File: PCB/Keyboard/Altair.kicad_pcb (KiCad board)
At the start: 2 copper layers, 57 parts, among them SW1 SW_Push, SW10 SW_Push, SW11 SW_Push, SW12 SW_Push, SW13 SW_Push, SW14 SW_Push, SW15 SW_Push, SW16 SW_Push, SW17 SW_Push, SW18 SW_Push, SW19 SW_Push, SW2 SW_Push, SW20 SW_Push, SW21 SW_Push, SW22 SW_Push, SW23 SW_Push, SW24 SW_Push, SW25 SW_Push, SW26 SW_Push, SW27 SW_Push, SW28 SW_Push, SW3 SW_Push, SW4 SW_Push, SW5 SW_Push, SW6 SW_Push, SW7 SW_Push, SW8 SW_Push, SW9 SW_Push, U1 SuperMini nRF52840

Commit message: add hs reverse fp
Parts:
- moved D4 6.87 mm to (144.4, 53.9)
- moved D3 6.52 mm to (125.1, 56.1)
- moved D12 6.02 mm to (181.7, 77.2)
- moved D11 5.94 mm to (162.4, 74.9)
- moved D5 5.21 mm to (162.9, 54.7)
- moved D6 4.64 mm to (181.6, 56.5)
- moved D1 2.24 mm to (84.6, 60.6)
- moved D2 1.94 mm to (87.2, 60.7)
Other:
- board outline added: 137.3 x 110.5 mm

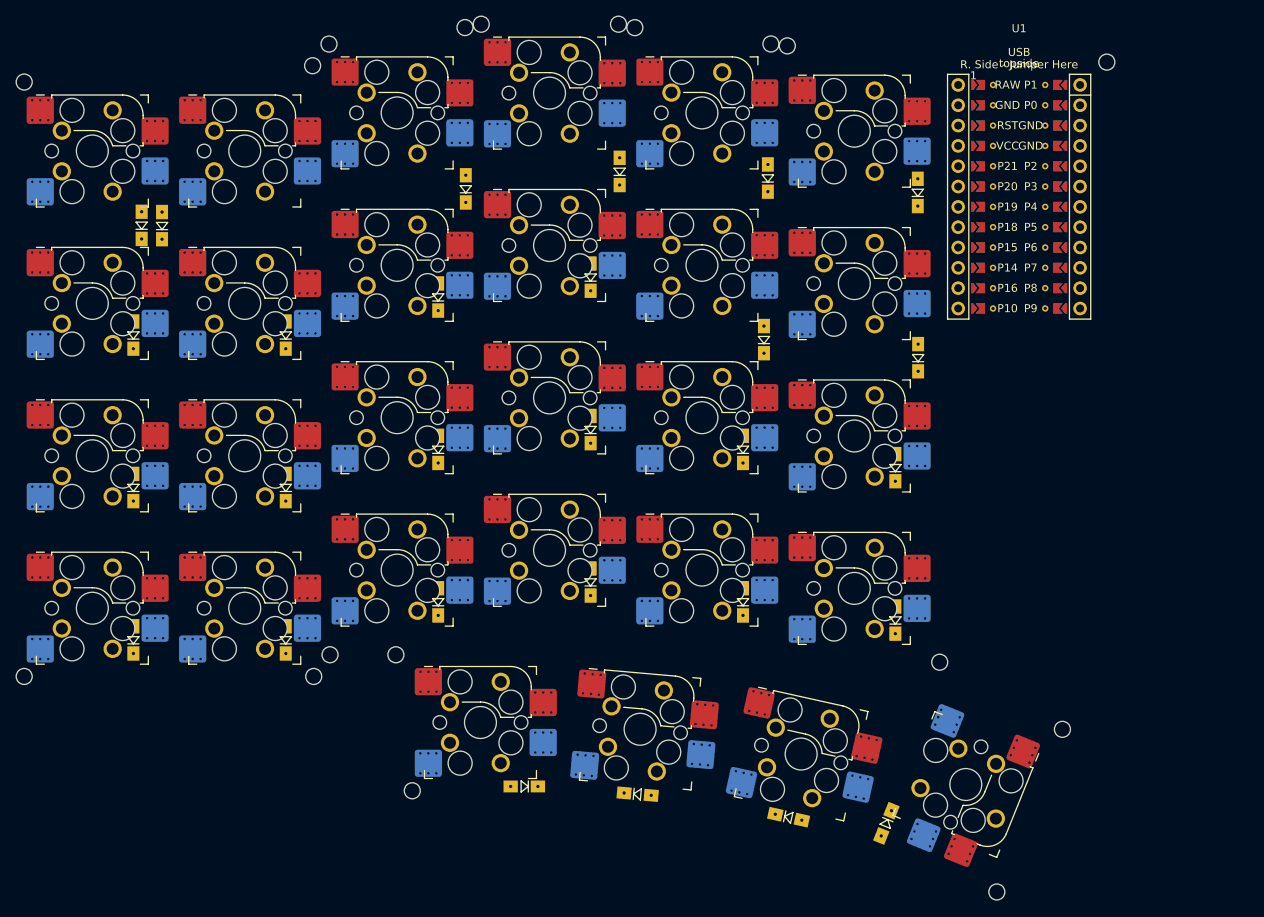
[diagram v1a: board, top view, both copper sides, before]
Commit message: Done outline and fp for mcu/switch
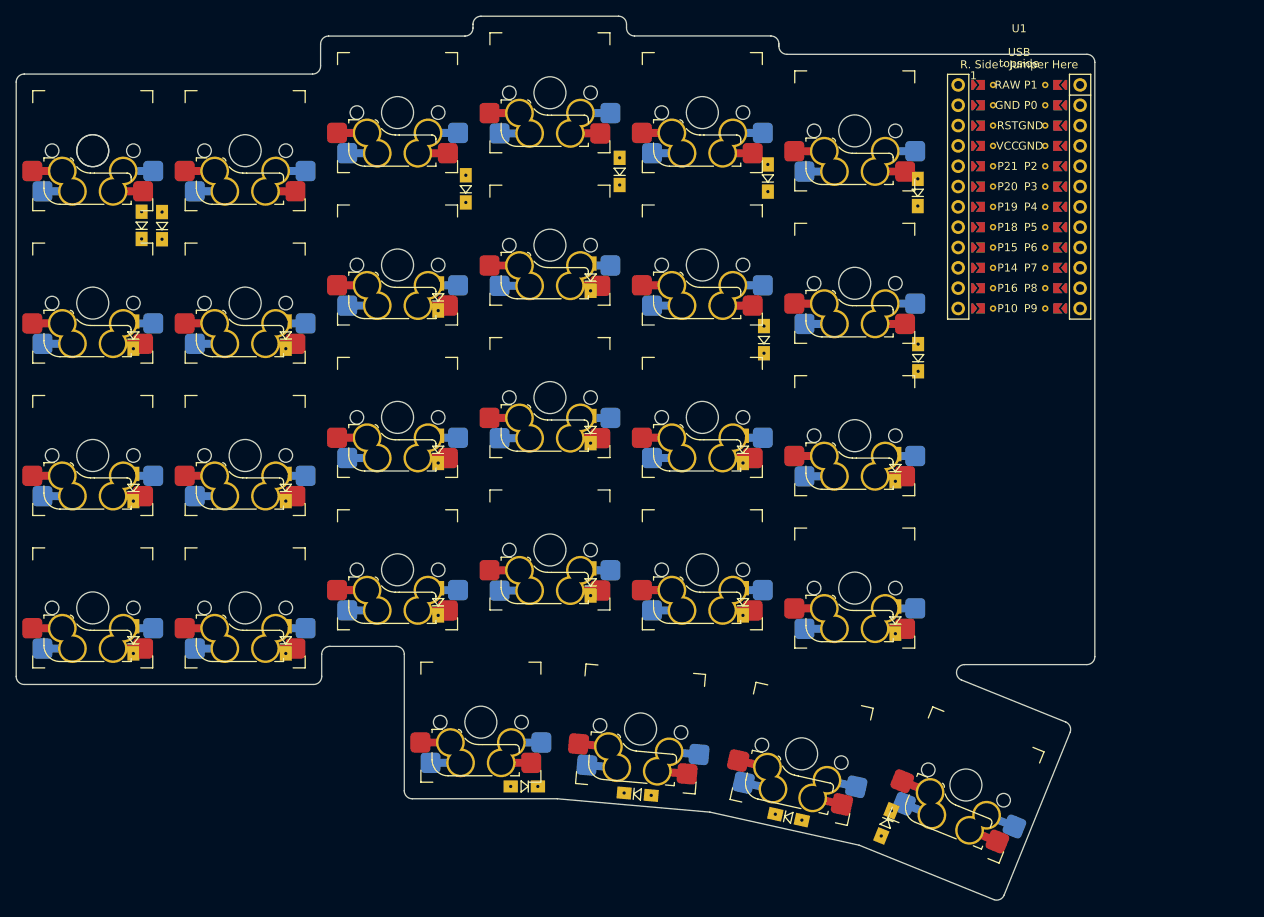
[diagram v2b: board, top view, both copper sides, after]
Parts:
- SW1, SW10, SW11, SW12, SW13, SW14, SW15, SW16, SW17, SW18, SW19, SW2, SW20, SW21, SW22, SW23, SW24, SW25, SW26, SW27, SW3, SW4, SW5, SW6, SW7, SW8, SW9: footprint MX_Optional_Reversible:MX-Optional-Reversible-1U -> hs:SW_MX_HotSwap_PTH_double
- SW28: footprint MX_Optional_Reversible:MX-Optional-Reversible-1.25U -> hs:SW_MX_HotSwap_PTH_double
- turned SW28 to -22 degrees
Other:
- board size 137.3 x 110.5 mm -> 134.8 x 110.5 mm

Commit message: routing sw
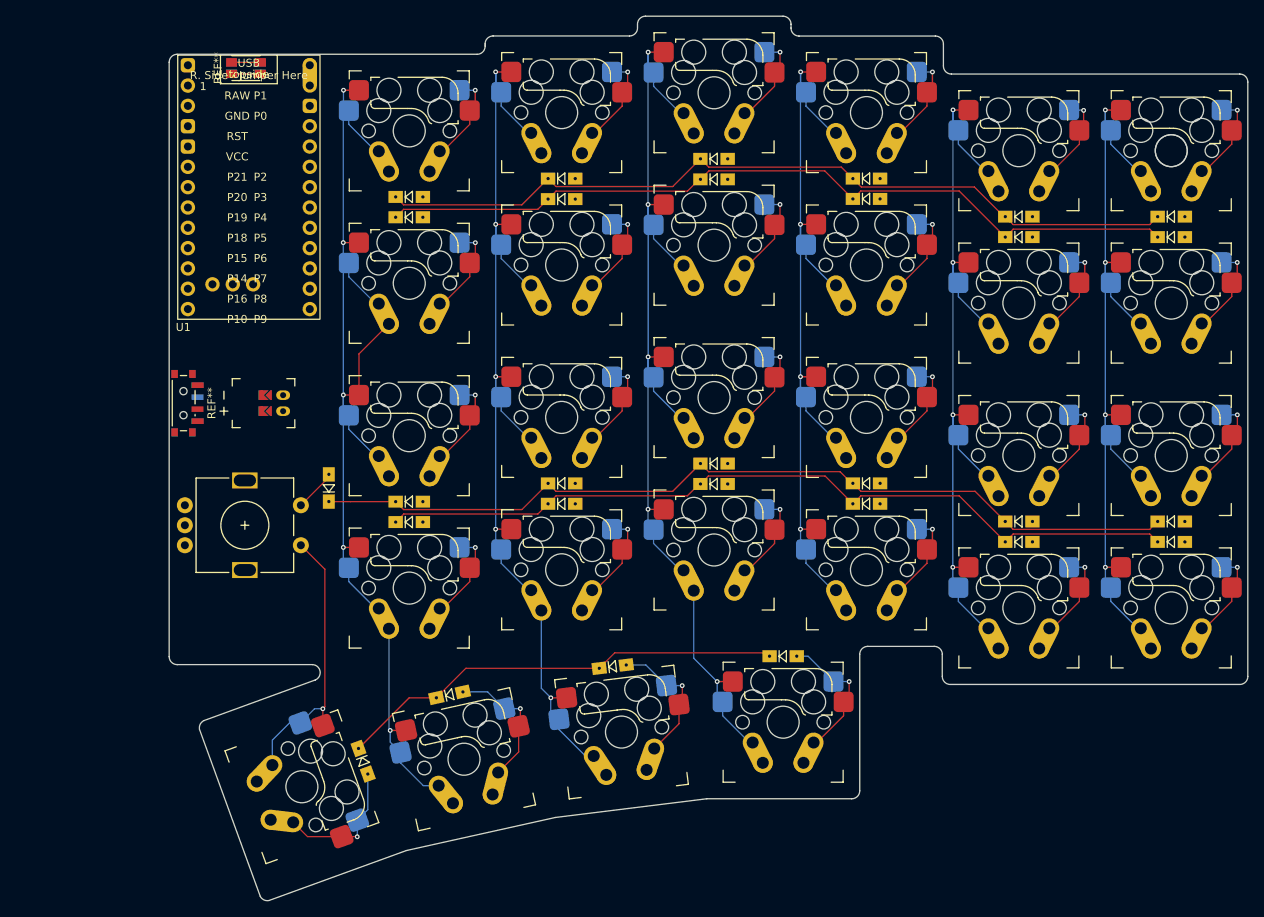
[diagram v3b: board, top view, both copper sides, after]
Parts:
- added D98: D, SofleKeyboard-footprint:Diode_SOD123, F.Cu at (108.0, 93.5)
- added J1: Conn_01x02_Socket, ergogen_fp:battery_connector_jst_ph_2, B.Cu at (102.3, 82.8)
- added SW97: SW_Nidec_CAS-120A1, ergogen_fp:sw_power, B.Cu at (89.9, 82.8)
- added SW98: RotaryEncoder_Switch, SofleKeyboard-footprint:RotaryEncoder_Alps_EC11E-Switch_Vertical_H20mm-keebio_modified, F.Cu at (97.5, 98.1)
- added SW99: SW_Push, ergogen_fp:sw_reset_side, B.Cu at (97.7, 41.0)
- D1, D10, D11, D12, D13, D14, D15, D16, D17, D18, D19, D2, D20, D21, D22, D23, D24, D25, D26, D27, D28, D3, D4, D5, D6, D7, D8, D9: moved to F.Cu
- SW1, SW10, SW11, SW12, SW13, SW14, SW15, SW16, SW17, SW18, SW19, SW2, SW20, SW21, SW22, SW23, SW24, SW25, SW26, SW27, SW28, SW3, SW4, SW5, SW6, SW7, SW8, SW9: footprint hs:SW_MX_HotSwap_PTH_double -> hs:SW_MX_HotSwap_THT_double; moved to B.Cu
- U1: footprint ergogen_fp:nice_nano -> PCM_marbastlib-xp-promicroish:SuperMini_nRF52840_AH_Reversible
- moved SW1 134.8 mm to (213.3, 51.3)
- moved SW13 134.8 mm to (213.3, 89.4)
- moved SW19 134.8 mm to (213.3, 108.4)
- moved SW7 134.8 mm to (213.3, 70.3)
- moved D19 130.3 mm to (213.3, 100.2), turned to 0 degrees
- moved D7 130.3 mm to (213.3, 62.1), turned to 0 degrees
- moved D13 129.8 mm to (213.3, 97.6), turned to 0 degrees
- moved D1 128.7 mm to (213.3, 59.5), turned to 0 degrees
- moved D2 107.1 mm to (194.3, 59.5), turned to 0 degrees
- moved SW14 96.7 mm to (194.3, 89.4)
- moved SW2 96.7 mm to (194.3, 51.3)
- moved SW20 96.7 mm to (194.3, 108.4)
- moved SW8 96.7 mm to (194.3, 70.3)
- moved U1 96.3 mm to (98.0, 57.1)
- moved D20 92.5 mm to (194.3, 100.2), turned to 0 degrees
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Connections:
- D28 pad 1: ROW5 -> ROW4
- U1 pad 11: unconnected-(U1-P1.04-LF-Pad11) -> Net-(SW97-B)
- U1 pad 14: unconnected-(U1-GND-Pad14) -> Net-(SW99-Pad1)
- U1 pad 15: unconnected-(U1-RST-Pad15) -> Net-(U1-RST)
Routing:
- net COL5: track 0.00 -> 136.7 mm, vias 0 -> 5
- net COL3: track 0.00 -> 128.0 mm, vias 0 -> 5
- net COL4: track 0.00 -> 127.3 mm, vias 0 -> 5
- net ROW2: track 0.00 -> 111.1 mm
- net COL0: track 0.00 -> 104.6 mm, vias 0 -> 4
- net COL1: track 0.00 -> 103.8 mm, vias 0 -> 4
- net COL2: track 0.00 -> 103.8 mm, vias 0 -> 4
- net ROW1: track 0.00 -> 102.7 mm
- net ROW3: track 0.00 -> 102.7 mm
- net ROW0: track 0.00 -> 102.7 mm
- net ROW4: track 0.00 -> 56.5 mm
- net COL6: track 0.00 -> 34.9 mm, vias 0 -> 1
- net N$25: track 0.00 -> 17.6 mm, vias 0 -> 1
- net N$26: track 0.00 -> 17.4 mm, vias 0 -> 1
- net N$27: track 0.00 -> 17.2 mm, vias 0 -> 1
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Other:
- board size 134.8 x 110.5 mm -> 134.8 x 110.6 mm

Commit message: inprocessing
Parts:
- SW97: moved to F.Cu
- SW99: footprint ergogen_fp:sw_reset_side -> kbd:ResetSW; moved to F.Cu
- moved SW99 34.9 mm to (97.9, 75.8), turned to 180 degrees
- moved SW97 1.25 mm to (90.0, 84.1)
- moved J1 1.24 mm to (102.3, 84.1)
- moved U1 0.19 mm to (97.9, 57.2)
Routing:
- net Net-(U1-RST): track 7.20 -> 0.00 mm
- net Net-(SW99-Pad1): track 7.20 -> 0.00 mm
- net N$9: track 11.7 -> 17.6 mm
- net N$24: track 11.7 -> 17.6 mm
- net N$12: track 11.7 -> 17.6 mm
- net N$22: track 11.7 -> 17.6 mm
- net N$19: track 11.7 -> 17.6 mm
- net N$7: track 11.6 -> 17.6 mm
- net N$20: track 11.7 -> 17.6 mm
- net N$8: track 11.6 -> 17.6 mm
- net N$23: track 11.7 -> 17.6 mm
- net N$21: track 11.6 -> 17.5 mm
- net N$11: track 11.7 -> 17.6 mm
- net N$10: track 11.7 -> 17.6 mm
- net N$4: track 11.7 -> 15.2 mm
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
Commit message: add sample
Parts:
- added J10, J12: Jumper, lib:Jumper, F.Cu at (100.3, 48.4)
- added J11: Jumper, lib:Jumper, F.Cu at (100.3, 45.8)
- added J13: Jumper, lib:Jumper, F.Cu at (100.3, 50.9)
- added J14, J8: Jumper, lib:Jumper, F.Cu at (95.3, 48.4)
- added J7: Jumper, lib:Jumper, F.Cu at (95.3, 45.8)
- added J9: Jumper, lib:Jumper, F.Cu at (95.3, 50.9)
- SW97, U1: moved to B.Cu
- moved SW97 43.4 mm to (97.9, 41.4), turned to 90 degrees
- turned U1 to 180 degrees
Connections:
- SW97 pad 5: (no net) -> unconnected-(U1-BAT+-Pad13)
- SW99 pad 1: Net-(SW99-Pad1) -> unconnected-(SW99-Pad1)
- U1 pad 14: Net-(SW99-Pad1) -> unconnected-(U1-GND-Pad14)
- U1 pad 28: (no net) -> unconnected-(U1-GND-Pad28)
- U1 pad 29: (no net) -> unconnected-(U1-BAT+-Pad29)
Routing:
- net unconnected-(U1-BAT+-Pad13): track 0.00 -> 21.3 mm, vias 0 -> 1
- net Net-(J1-Pin_2): track 0.00 -> 20.0 mm
- net Net-(U1-RST): track 0.00 -> 6.84 mm, vias 0 -> 1
- net unconnected-(U1-GND-Pad3): track 0.00 -> 6.69 mm, vias 0 -> 1

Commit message: inprocess
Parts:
- SW99: moved to B.Cu
- moved J1 13.6 mm to (90.6, 77.2), turned to -90 degrees
- moved SW99 8.36 mm to (97.9, 84.2), turned to 0 degrees
- moved D98 3.98 mm to (108.1, 97.4), turned to -90 degrees
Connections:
- J1 pad 1: Net-(J1-Pin_1) -> unconnected-(J1-Pin_1-Pad1)
- J1 pad 2: Net-(J1-Pin_2) -> unconnected-(J1-Pin_2-Pad2)
- SW97 pad 1: Net-(J1-Pin_2) -> unconnected-(SW97-C-Pad1)
- SW97 pad 2: Net-(SW97-B) -> unconnected-(SW97-B-Pad2)
- SW97 pad 3: Net-(J1-Pin_1) -> unconnected-(SW97-A-Pad3)
- SW97 pad 5: unconnected-(U1-BAT+-Pad13) -> (no net)
- SW98 pad A: unconnected-(SW98-PadA) -> EC_A
- SW98 pad B: unconnected-(SW98-PadB) -> EC_B
- SW98 pad C: unconnected-(SW98-PadC) -> EC_C
- SW99 pad 1: unconnected-(SW99-Pad1) -> Net-(U1-RST)
- SW99 pad 2: Net-(U1-RST) -> unconnected-(U1-GND-Pad3)
- U1 pad 10: unconnected-(U1-P0.11-Pad10) -> EC_B
- U1 pad 11: Net-(SW97-B) -> EC_C
- U1 pad 12: unconnected-(U1-P1.06-LF-Pad12) -> EC_A
- U1 pad 14: unconnected-(U1-GND-Pad14) -> GND
- U1 pad 15: Net-(U1-RST) -> RST
- U1 pad 18: ROW1 -> COL4
- U1 pad 19: ROW2 -> ROW1
- U1 pad 20: ROW3 -> COL5
- U1 pad 21: ROW4 -> COL0
- U1 pad 22: unconnected-(U1-P1.11-LF-Pad22) -> COL1
- U1 pad 23: unconnected-(U1-P0.10-LF-Pad23) -> COL2
- U1 pad 24: unconnected-(U1-P0.09-LF-Pad24) -> COL3
- U1 pad 28: unconnected-(U1-GND-Pad28) -> GND
- U1 pad 3: unconnected-(U1-GND-Pad3) -> GND
- U1 pad 4: unconnected-(U1-GND-Pad4) -> GND
- U1 pad 6: unconnected-(U1-P0.20-Pad6) -> ROW2
- U1 pad 7: unconnected-(U1-P0.22-Pad7) -> ROW3
- U1 pad 8: unconnected-(U1-P0.24-Pad8) -> ROW4
- U1 pad 9: unconnected-(U1-P1.00-Pad9) -> COL6
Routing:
- net COL0: track 104.6 -> 220.4 mm, vias 4 -> 5
- net COL1: track 103.8 -> 202.0 mm, vias 4 -> 5
- net ROW4: track 56.5 -> 131.9 mm
- net COL2: track 103.8 -> 175.7 mm, vias 4 -> 5
- net ROW3: track 102.7 -> 158.0 mm
- net COL3: track 128.0 -> 176.5 mm, vias 5 -> 6
- net ROW2: track 111.1 -> 159.2 mm
- net COL6: track 35.2 -> 79.3 mm
- net EC_B: track 0.00 -> 38.6 mm
- net EC_C: track 0.00 -> 33.0 mm
- net EC_A: track 0.00 -> 25.3 mm
- net COL4: track 127.3 -> 152.5 mm
- net Net-(J1-Pin_2): track 20.0 -> 0.00 mm
- net GND: track 0.00 -> 20.0 mm
- net ROW0: track 102.7 -> 115.1 mm
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
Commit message: done & clean
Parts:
- removed U1: SuperMini nRF52840, PCM_marbastlib-xp-promicroish:SuperMini_nRF52840_AH_Reversible
- added ?: , lib:niceview_headers, B.Cu at (97.9, 40.2)
- added MCU1: , ProMicro, B.Cu at (97.9, 57.2)
- PWR: renamed from SW97; moved to F.Cu
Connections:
- J1 pad 1: unconnected-(J1-Pin_1-Pad1) -> GND
- J1 pad 2: unconnected-(J1-Pin_2-Pad2) -> GND
- J10 pad 1: (no net) -> RST_GND
- J10 pad 2: (no net) -> GND
- J11 pad 1: unconnected-(U1-BAT+-Pad13) -> RAW_P1
- J11 pad 2: (no net) -> RAW
- J12 pad 1: Net-(U1-RST) -> RST_GND
- J12 pad 2: Net-(U1-RST) -> RST
- J13 pad 1: (no net) -> VCC_GND
- J13 pad 2: (no net) -> VCC
- J14 pad 1: unconnected-(U1-GND-Pad3) -> GND_RST
- J14 pad 2: unconnected-(U1-GND-Pad3) -> GND
- J7 pad 1: unconnected-(U1-BAT+-Pad13) -> P1_RAW
- J7 pad 2: unconnected-(U1-BAT+-Pad13) -> RAW
- J8 pad 1: (no net) -> GND_RST
- J8 pad 2: (no net) -> RST
- J9 pad 1: (no net) -> GND_VCC
- J9 pad 2: (no net) -> VCC
- PWR pad 1: unconnected-(SW97-C-Pad1) -> switch_from
- PWR pad 2: unconnected-(SW97-B-Pad2) -> RAW
- SW98 pad C: EC_C -> GND
- SW99 pad 1: Net-(U1-RST) -> RST
- SW99 pad 2: unconnected-(U1-GND-Pad3) -> GND
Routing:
- net GND: track 20.0 -> 85.2 mm, vias 0 -> 2
- net RST: track 0.00 -> 41.0 mm, vias 0 -> 1
- net VCC: track 0.00 -> 39.9 mm, vias 0 -> 4
- net EC_C: track 33.0 -> 0.00 mm
- net unconnected-(U1-BAT+-Pad13): track 21.3 -> 0.00 mm, vias 1 -> 0
- net switch_from: track 0.00 -> 19.0 mm
- net EC_A: track 25.3 -> 35.7 mm
- net RST_GND: track 0.00 -> 9.48 mm
- net RAW: track 0.00 -> 9.16 mm, vias 0 -> 1
- net GND_RST: track 0.00 -> 9.01 mm
- net COL6: track 79.3 -> 71.2 mm
- net ROW2: track 159.2 -> 151.6 mm
- net ROW3: track 158.0 -> 150.3 mm
- net ROW4: track 131.9 -> 124.3 mm
- net Net-(U1-RST): track 6.84 -> 0.00 mm, vias 1 -> 0
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- added copper zone on B.Cu, net GND
- added copper zone on F.Cu, net GND
